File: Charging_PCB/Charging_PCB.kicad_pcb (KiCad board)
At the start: 2 copper layers, 80 x 60 mm, 18 parts, among them K101 Relay_SPDT_Omron_G2RL-1, K102 Relay_SPDT_Omron_G2RL-1, Q101 Q_PMOS_GSD, Q102 Q_PMOS_GSD, U101 641964-1, U102 641964-1, U103 641964-1

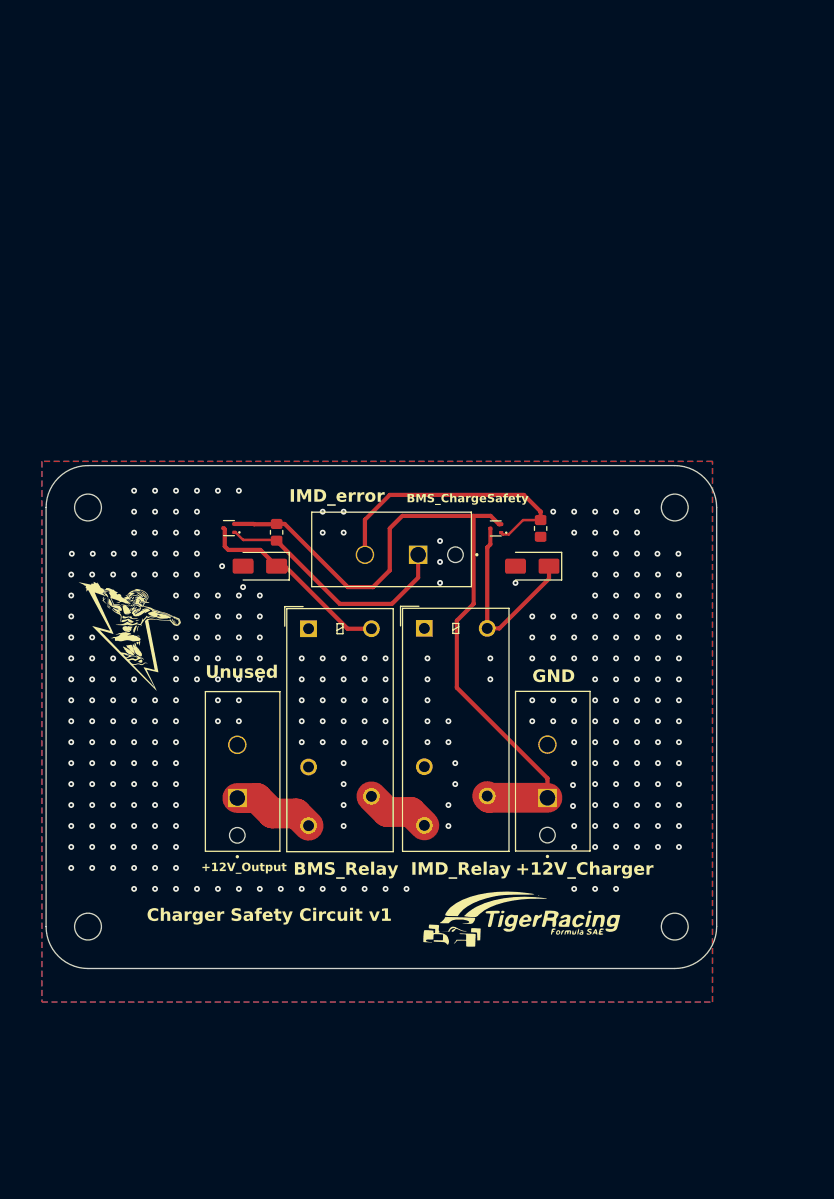
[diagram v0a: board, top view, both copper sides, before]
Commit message: Finished schematic with added SR latch and new buttons, started layout
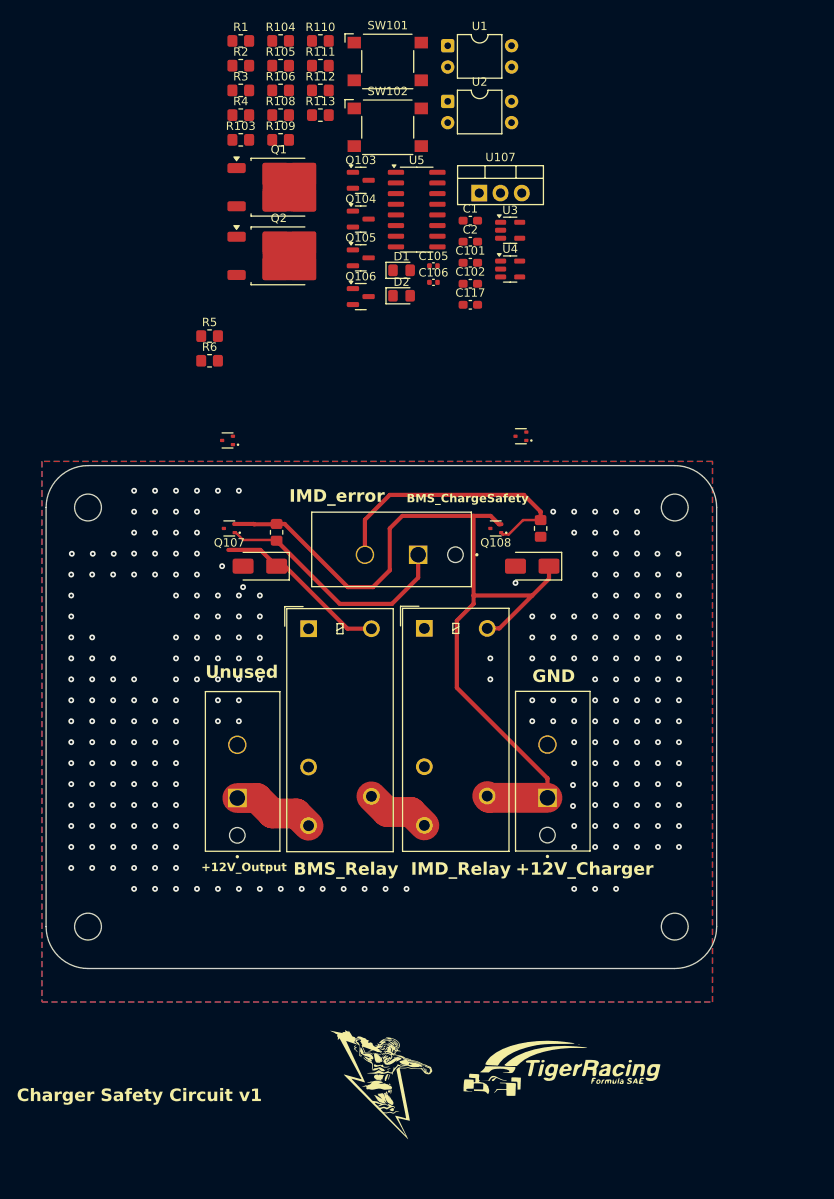
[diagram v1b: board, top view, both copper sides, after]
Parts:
- added C1: 100n, Capacitor_SMD:C_0603_1608Metric_Pad1.08x0.95mm_HandSolder, F.Cu at (157.6, 45.3)
- added C101: 10n, Capacitor_SMD:C_0603_1608Metric_Pad1.08x0.95mm_HandSolder, F.Cu at (157.6, 50.3)
- added C102: 10n, Capacitor_SMD:C_0603_1608Metric_Pad1.08x0.95mm_HandSolder, F.Cu at (157.6, 52.8)
- added C105: 0.33u, Capacitor_SMD:C_0402_1005Metric, F.Cu at (153.2, 50.7)
- added C106: 0.01u, Capacitor_SMD:C_0402_1005Metric, F.Cu at (153.2, 52.6)
- added C117: 100n, Capacitor_SMD:C_0603_1608Metric_Pad1.08x0.95mm_HandSolder, F.Cu at (157.6, 55.3)
- added C2: 100n, Capacitor_SMD:C_0603_1608Metric_Pad1.08x0.95mm_HandSolder, F.Cu at (157.6, 47.8)
- added D1: LED, LED_SMD:LED_0805_2012Metric_Pad1.15x1.40mm_HandSolder, F.Cu at (149.4, 51.2)
- added D2: LED, LED_SMD:LED_0805_2012Metric_Pad1.15x1.40mm_HandSolder, F.Cu at (149.4, 54.2)
- added Q1: NMOS, Package_TO_SOT_SMD:TO-252-2, F.Cu at (134.8, 41.3)
- added Q103: Q_NPN_BEC, Package_TO_SOT_SMD:SOT-23, F.Cu at (144.5, 40.5)
- added Q104: Q_NPN_BEC, Package_TO_SOT_SMD:SOT-23, F.Cu at (144.5, 45.1)
- added Q105: Q_NPN_BEC, Package_TO_SOT_SMD:SOT-23, F.Cu at (144.5, 49.7)
- added Q106: Q_NPN_BEC, Package_TO_SOT_SMD:SOT-23, F.Cu at (144.5, 54.3)
- added Q107: Q_PMOS_GSD, Library:SOT-523_Custom(C96676), F.Cu at (128.9, 82.0)
- added Q108: Q_PMOS_GSD, Library:SOT-523_Custom(C96676), F.Cu at (160.6, 82.0)
- added Q2: NMOS, Package_TO_SOT_SMD:TO-252-2, F.Cu at (134.8, 49.5)
- added R1: 10k, Resistor_SMD:R_0805_2012Metric_Pad1.20x1.40mm_HandSolder, F.Cu at (130.2, 23.8)
- added R103: 100k, Resistor_SMD:R_0805_2012Metric_Pad1.20x1.40mm_HandSolder, F.Cu at (130.2, 35.6)
- added R104: 100k, Resistor_SMD:R_0805_2012Metric_Pad1.20x1.40mm_HandSolder, F.Cu at (135.0, 23.8)
- added R105: 10k, Resistor_SMD:R_0805_2012Metric_Pad1.20x1.40mm_HandSolder, F.Cu at (135.0, 26.8)
- added R106: 10k, Resistor_SMD:R_0805_2012Metric_Pad1.20x1.40mm_HandSolder, F.Cu at (135.0, 29.7)
- added R108: 1k, Resistor_SMD:R_0805_2012Metric_Pad1.20x1.40mm_HandSolder, F.Cu at (135.0, 32.7)
- added R109: 1k, Resistor_SMD:R_0805_2012Metric_Pad1.20x1.40mm_HandSolder, F.Cu at (135.0, 35.6)
- added R110: 100k, Resistor_SMD:R_0805_2012Metric_Pad1.20x1.40mm_HandSolder, F.Cu at (139.7, 23.8)
- added R111: 1k, Resistor_SMD:R_0805_2012Metric_Pad1.20x1.40mm_HandSolder, F.Cu at (139.7, 26.8)
- added R112: 100k, Resistor_SMD:R_0805_2012Metric_Pad1.20x1.40mm_HandSolder, F.Cu at (139.7, 29.7)
- added R113: 1k, Resistor_SMD:R_0805_2012Metric_Pad1.20x1.40mm_HandSolder, F.Cu at (139.7, 32.7)
- added R2: 10k, Resistor_SMD:R_0805_2012Metric_Pad1.20x1.40mm_HandSolder, F.Cu at (130.2, 26.8)
- added R3: 270, Resistor_SMD:R_0805_2012Metric_Pad1.20x1.40mm_HandSolder, F.Cu at (130.2, 29.7)
- added R4: 270, Resistor_SMD:R_0805_2012Metric_Pad1.20x1.40mm_HandSolder, F.Cu at (130.2, 32.7)
- added R5: 10k, Resistor_SMD:R_0805_2012Metric_Pad1.20x1.40mm_HandSolder, F.Cu at (126.5, 59.0)
- added R6: 10k, Resistor_SMD:R_0805_2012Metric_Pad1.20x1.40mm_HandSolder, F.Cu at (126.5, 62.0)
- added SW101: SW_Omron_B3FS, Button_Switch_SMD:SW_SPST_Omron_B3FS-100xP, F.Cu at (147.8, 26.3)
- added SW102: SW_Omron_B3FS, Button_Switch_SMD:SW_SPST_Omron_B3FS-100xP, F.Cu at (147.8, 34.1)
- added U1: SFH617A-1, Package_DIP:DIP-4_W7.62mm, F.Cu at (154.9, 24.4)
- added U107: LM7805_TO220, Package_TO_SOT_THT:TO-220-3_Vertical, F.Cu at (158.7, 42.0)
- added U2: SFH617A-1, Package_DIP:DIP-4_W7.62mm, F.Cu at (154.9, 31.1)
- added U3: 74AHC1G00, Package_TO_SOT_SMD:SOT-23-5, F.Cu at (162.4, 46.4)
- added U4: 74AHC1G00, Package_TO_SOT_SMD:SOT-23-5, F.Cu at (162.4, 51.0)
- added U5: 74LS279, Package_SO:SOIC-16_3.9x9.9mm_P1.27mm, F.Cu at (151.2, 44.0)
- moved G*** 61.3 mm to (147.0, 148.0)
- moved G*** 18.4 mm to (160.3, 147.9)
- moved G*** 18.4 mm to (168.5, 146.5)
- moved Q102 11.4 mm to (163.6, 71.0)
- moved Q101 10.5 mm to (128.6, 71.5)
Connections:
- D101 pad 1: Net-(D101-K) -> +12V
- D101 pad 2: GND -> Net-(D101-A)
- D102 pad 1: Net-(D102-K) -> +12V
- D102 pad 2: GND -> Net-(D102-A)
- K101 pad A1: GND -> Net-(D101-A)
- K101 pad A2: Net-(D101-K) -> +12V
- K102 pad A1: GND -> Net-(D102-A)
- K102 pad A2: Net-(D102-K) -> +12V
- Q101 pad 1: /BMS_CSO -> Net-(Q101-G)
- Q101 pad 3: Net-(D101-K) -> Net-(Q101-D)
- Q102 pad 1: /IMD_Error -> Net-(Q102-G)
- Q102 pad 3: Net-(D102-K) -> Net-(Q102-D)
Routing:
- net +12V: track 88.2 -> 127.5 mm
- net Net-(D101-K): track 23.8 -> 0.00 mm
- net Net-(D102-K): track 23.4 -> 0.00 mm
- net GND: vias 295 -> 248

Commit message: Added SR Latch to charging PCB, completed gerbers,bom,and CPL file and added mouser parts list to assembly file
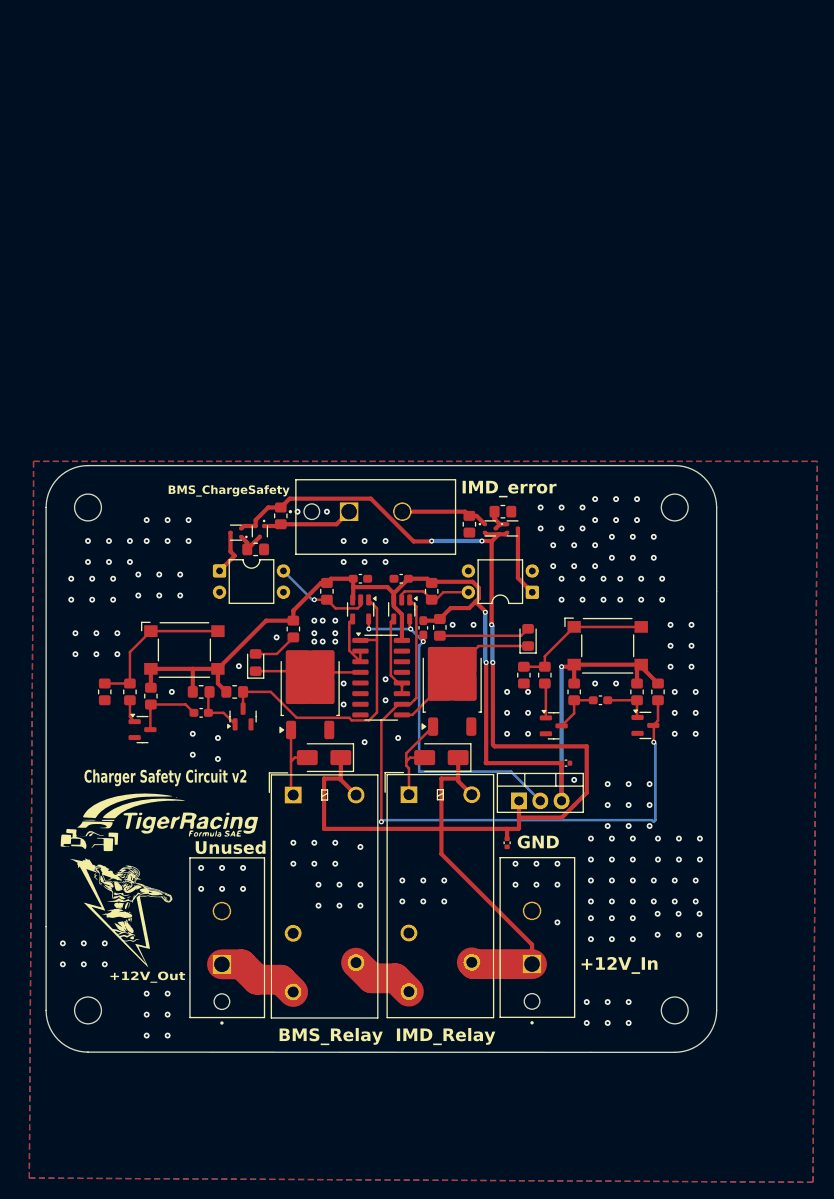
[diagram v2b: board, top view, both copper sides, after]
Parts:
- moved R112 81.1 mm to (177.5, 101.5), turned to -90 degrees
- moved R104 81.0 mm to (164.0, 99.5), turned to -90 degrees
- moved R113 79.7 mm to (180.0, 101.5), turned to -90 degrees
- moved R110 79.0 mm to (125.5, 101.5)
- moved R105 76.8 mm to (117.0, 101.5), turned to 90 degrees
- moved R106 76.6 mm to (166.5, 99.5), turned to 90 degrees
- moved R111 75.4 mm to (129.5, 101.5)
- moved R109 74.6 mm to (170.0, 101.5), turned to -90 degrees
- moved SW101 74.3 mm to (123.5, 96.5)
- moved U107 72.7 mm to (163.4, 114.5)
- moved R108 71.0 mm to (119.5, 102.0), turned to -90 degrees
- moved Q103 70.5 mm to (118.5, 106.0)
- moved C105 69.4 mm to (162.0, 119.5), turned to -90 degrees
- moved U1 68.3 mm to (127.7, 87.1)
- moved R103 67.8 mm to (114.0, 101.5), turned to -90 degrees
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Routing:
- net +5V: track 0.00 -> 138.9 mm, vias 0 -> 3
- net /IMD_RESET: track 0.00 -> 76.9 mm, vias 0 -> 2
- net +12V: track 127.5 -> 170.5 mm, vias 0 -> 4
- net GND: track 0.00 -> 42.0 mm, vias 248 -> 216
- net /BMS_RESET: track 0.00 -> 35.6 mm
- net /IMD_Error: track 33.7 -> 10.5 mm
- net Net-(R103-Pad1): track 0.00 -> 18.3 mm
- net /BMS_CSO: track 29.5 -> 11.3 mm
- net Net-(R104-Pad1): track 0.00 -> 16.7 mm
- net Net-(D2-K): track 0.00 -> 14.0 mm
- net Net-(R1-Pad2): track 0.00 -> 12.3 mm, vias 0 -> 1
- net Net-(D102-A): track 0.00 -> 12.0 mm
- net Net-(D2-A): track 0.00 -> 10.9 mm
- net Net-(D1-K): track 0.00 -> 10.3 mm
- net Net-(U3-Pad4): track 0.00 -> 10.0 mm
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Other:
- board size 80 x 60 mm -> 80 x 70 mm
- board text added: "+12V_In"
- board text added: "+12V_Out"
- board text added: "Charger Safety Circuit v2"
- board text removed: "+12V_Charger"
- board text removed: "+12V_Output"
- board text removed: "Charger Safety Circuit v1"
